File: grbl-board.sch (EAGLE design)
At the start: 49 parts, among them IC1 MEGA328-P, IC2 FT232RL, IC3 ADuM1201AR, IC4 LM2596S, Q1 16 MHz, X1 PN61729-S

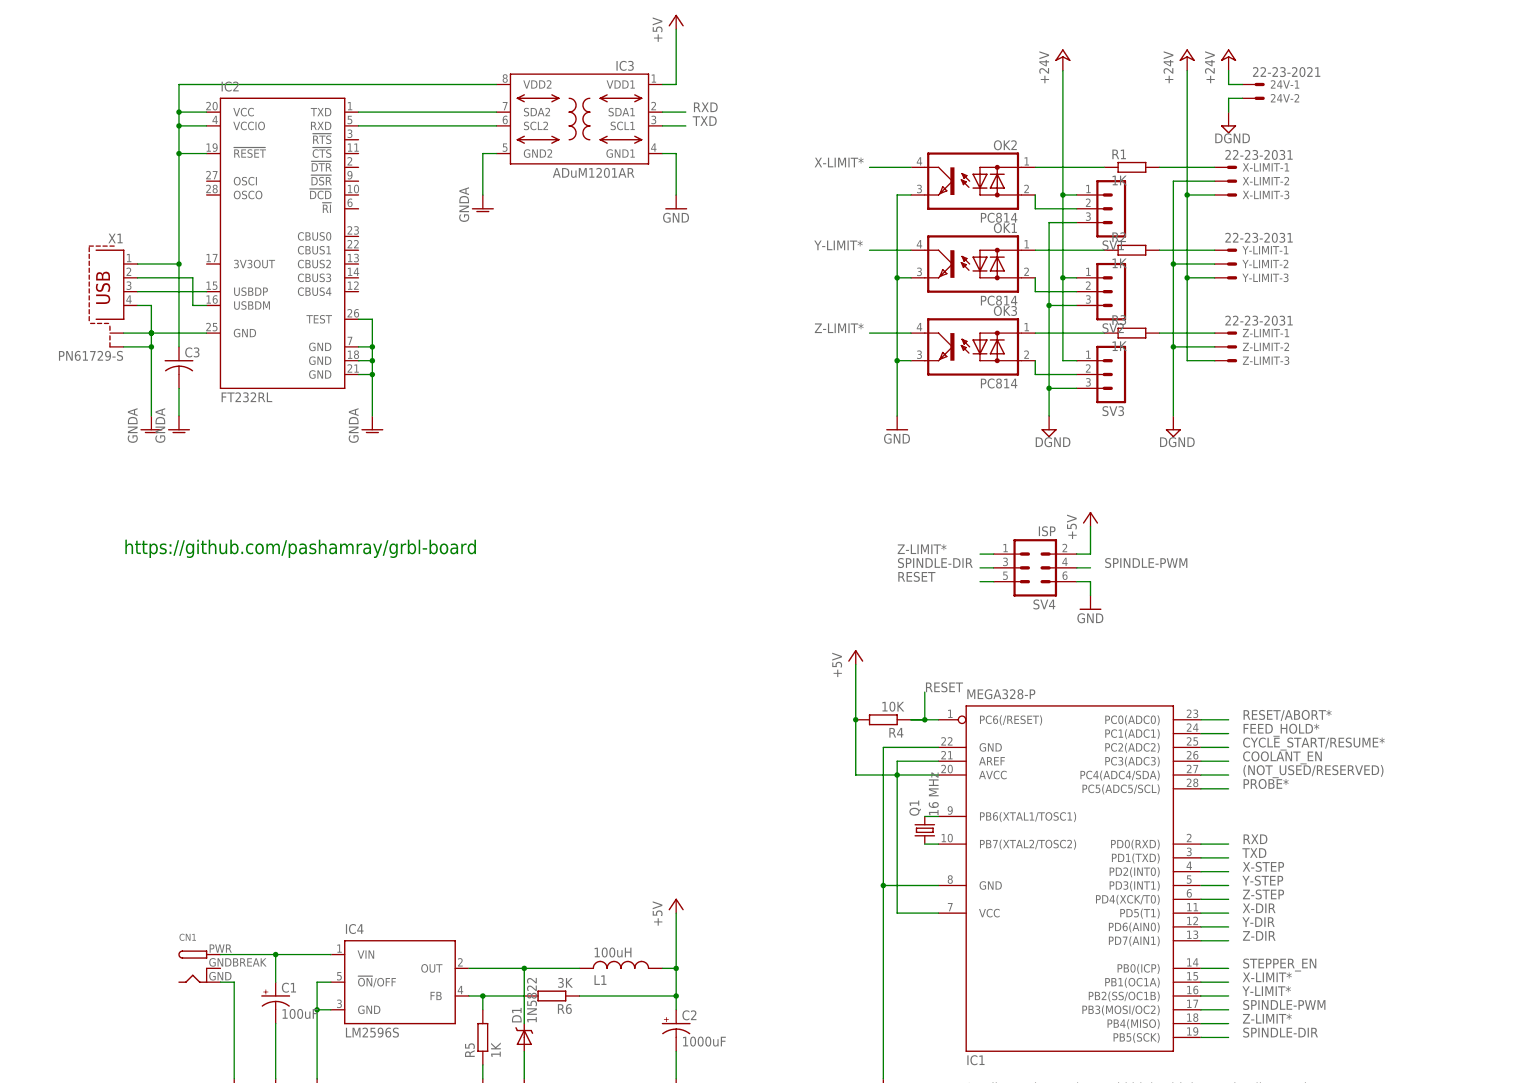
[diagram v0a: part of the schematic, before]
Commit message: route power supply
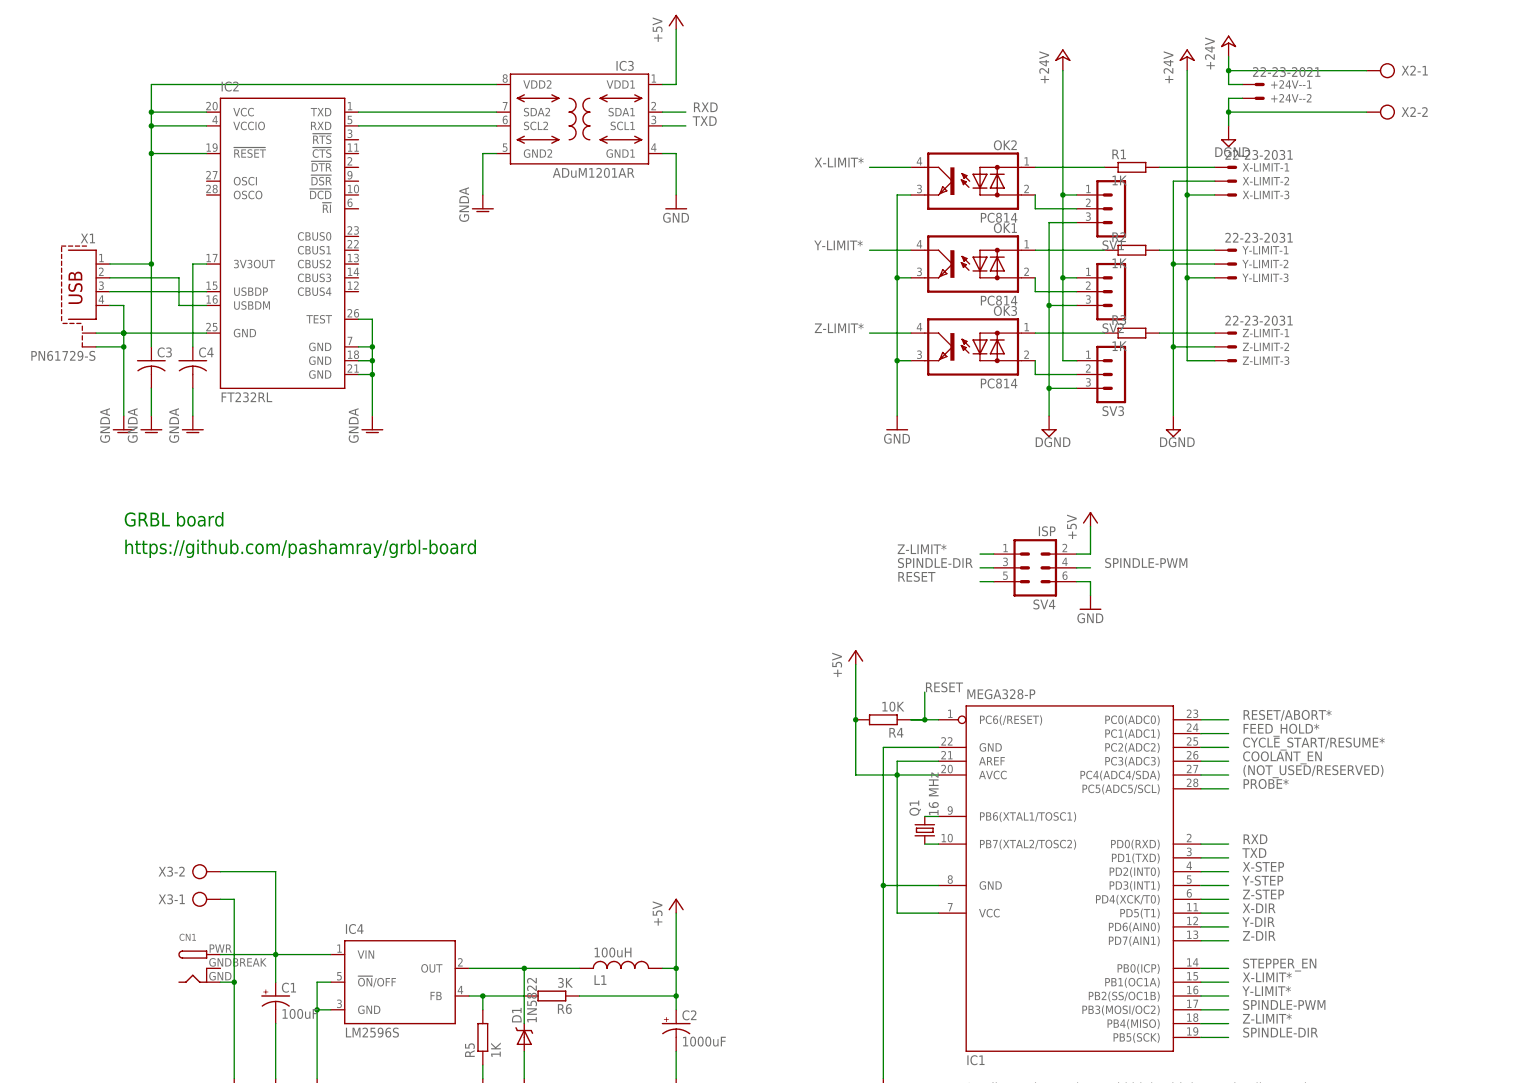
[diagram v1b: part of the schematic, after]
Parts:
- added C4: (no value), adafruit:C-USC0805K
- added X2, X3: (no value), con-ptr500:AK500/2
- C1: device adafruit:CPOL-USE5-10.5 -> adafruit:CPOL-USE5-6
- renumbered 24V to +24V-
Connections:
- new net N$31: C4.1, IC2.3V3OUT
- net +24V: now also X2-1.KL
- net DGND: now also X2-2.KL
- net GND: now also X3-1.KL
- net GNDA: now also C4.2
- net N$19: now also X3-2.KL
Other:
- note added: "GRBL board"
- moved on the sheet: C3, X1

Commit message: route round lines refactor
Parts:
- removed X3: (no value), con-ptr500:AK500/2
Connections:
- net GND: no longer X3-1.KL
- net N$19: no longer X3-2.KL
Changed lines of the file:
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@@
 <part name="GND8" library="supply1" deviceset="GNDA" device=""/>
 <part name="X2" library="con-ptr500" deviceset="AK500/2" device=""/>
-<part name="X3" library="con-ptr500" deviceset="AK500/2" device=""/>
 <part name="C4" library="adafruit" deviceset="C-US" device="C0805K"/>
 <part name="GND9" library="supply1" deviceset="GNDA" device=""/>
@@
 <instance part="X2" gate="-1" x="307.34" y="256.54" rot="MR0"/>
 <instance part="X2" gate="-2" x="307.34" y="248.92" rot="MR0"/>
-<instance part="X3" gate="-1" x="86.36" y="104.14"/>
-<instance part="X3" gate="-2" x="86.36" y="109.22"/>
 <instance part="C4" gate="G$1" x="86.36" y="203.2"/>
 <instance part="GND9" gate="1" x="86.36" y="190.5"/>
@@
 <wire x1="91.44" y1="88.9" x2="93.98" y2="88.9" width="0.1524" layer="91"/>
 <wire x1="93.98" y1="88.9" x2="93.98" y2="71.12" width="0.1524" layer="91"/>
-<wire x1="93.98" y1="104.14" x2="93.98" y2="88.9" width="0.1524" layer="91"/>
-<junction x="93.98" y="88.9"/>
-<pinref part="X3" gate="-1" pin="KL"/>
-<wire x1="93.98" y1="104.14" x2="91.44" y2="104.14" width="0.1524" layer="91"/>
 </segment>
 <segment>
@@
 <wire x1="101.6" y1="88.9" x2="101.6" y2="93.98" width="0.1524" layer="91"/>
 <junction x="101.6" y="93.98"/>
-<wire x1="101.6" y1="109.22" x2="101.6" y2="93.98" width="0.1524" layer="91"/>
-<pinref part="X3" gate="-2" pin="KL"/>
-<wire x1="101.6" y1="109.22" x2="91.44" y2="109.22" width="0.1524" layer="91"/>
-</segment>
-</net>
+</segment>
+</net>

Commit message: refactor
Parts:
- removed X-DRIVER, Y-DRIVER, Z-DRIVER: 22-23-2051, con-molex:22-23-2051
- added X, Y, Z: 22-23-2041, con-molex:22-23-2041
- SPINDLE: value 22-23-2051 -> 22-23-2041; device con-molex:22-23-2051 -> con-molex:22-23-2041
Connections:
- net +5V: no longer SPINDLE-1.S, SV4.2, X-DRIVER-1.S, Y-DRIVER-1.S, Z-DRIVER-1.S
- net COOLANT_EN: now also SPINDLE-1.S; no longer SPINDLE-5.S
- net GND: now also SPINDLE-4.S, X-4.S, Y-4.S, Z-4.S; no longer SPINDLE-2.S, X-DRIVER-2.S, Y-DRIVER-2.S, Z-DRIVER-2.S
- net SPINDLE-DIR: now also SPINDLE-2.S; no longer SPINDLE-4.S
- net STEPPER_EN: now also X-3.S, Y-3.S, Z-3.S; no longer X-DRIVER-5.S, Y-DRIVER-5.S, Z-DRIVER-5.S
- net X-DIR: now also IC1.PD3(INT1), X-2.S; no longer IC1.PD5(T1), X-DRIVER-4.S
- net X-STEP: now also X-1.S; no longer X-DRIVER-3.S
- net Y-DIR: now also IC1.PD5(T1), Y-2.S; no longer IC1.PD6(AIN0), Y-DRIVER-4.S
- net Y-STEP: now also IC1.PD4(XCK/T0), Y-1.S; no longer IC1.PD3(INT1), Y-DRIVER-3.S
- net Z-DIR: now also Z-2.S; no longer Z-DRIVER-4.S
- net Z-STEP: now also IC1.PD6(AIN0), Z-1.S; no longer IC1.PD4(XCK/T0), Z-DRIVER-3.S
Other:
- moved on the sheet: SPINDLE-1, SPINDLE-2, SPINDLE-3, SPINDLE-4

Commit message: ver.1.0
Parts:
- removed SV4: ISP, con-ml:ML6
- added C5, C6: (no value), adafruit:C-USC0805K
- added COOLANT_EN: 22-23-2031, con-molex:22-23-2031
- added OK8: PC817, optocoupler:PC817
- added R11: 1K, resistor:R-EU_M0805
- SPINDLE: value 22-23-2041 -> 22-23-2031; device con-molex:22-23-2041 -> con-molex:22-23-2031
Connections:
- new net N$32: OK8.COL, R11.1
- new net N$33: COOLANT_EN-1.S, R11.2
- net +24V: now also COOLANT_EN-3.S
- net COOLANT_EN: now also OK8.A; no longer SPINDLE-1.S
- net DGND: now also COOLANT_EN-2.S, OK8.EMIT
- net GND: now also C5.1, C6.1, OK8.C, SPINDLE-3.S; no longer SPINDLE-4.S, SV4.6
- net N$6: now also C5.2
- net N$7: now also C6.2
- net RESET: no longer SV4.5
- net SPINDLE-DIR: now also SPINDLE-1.S; no longer SPINDLE-2.S, SV4.3
- net SPINDLE-PWM: now also SPINDLE-2.S; no longer SPINDLE-3.S, SV4.4
- net Z-LIMIT*: no longer SV4.1
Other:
- moved on the sheet: Q1, SPINDLE-1, SPINDLE-2, SPINDLE-3
